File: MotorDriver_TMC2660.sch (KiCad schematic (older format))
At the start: 17 parts, among them U4 TMC2660

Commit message: Routing is complete.
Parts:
- C7: footprint Capacitor_SMD:C_0603_1608Metric -> Capacitor_SMD:C_0402_1005Metric
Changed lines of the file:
@@
 AR Path="/5AC337B6/5ACE1C6D/5ACC0B66/5AC338BF" Ref="U7"  Part="1"
 AR Path="/5AC337B6/5AD9F95A/5AD4B0F5/5AC338BF" Ref="U8"  Part="1"
-F 0 "U4" H 4875 2520 60  0000 C CNN
+F 0 "U8" H 4875 2520 60  0000 C CNN
 F 1 "TMC2660" H 4875 2414 60  0000 C CNN
 F 2 "PrntrBoardV1:TMC2660" H 4900 3600 60  0001 C CNN
@@
 AR Path="/5AC337B6/5ACE1C6D/5ACC0B66/5AC33A94" Ref="C50"  Part="1"
 AR Path="/5AC337B6/5AD9F95A/5AD4B0F5/5AC33A94" Ref="C64"  Part="1"
-F 0 "C7" H 4650 1800 50  0000 L CNN
+F 0 "C64" H 4650 1800 50  0000 L CNN
 F 1 "0.1uF 50V" H 4350 1550 50  0000 L CNN
-F 2 "Capacitor_SMD:C_0603_1608Metric" H 4638 1550 50  0001 C CNN
+F 2 "Capacitor_SMD:C_0402_1005Metric" H 4638 1550 50  0001 C CNN
 F 3 "~" H 4600 1700 50  0001 C CNN
 	1    4600 1700
@@
 AR Path="/5AC337B6/5ACE1C6D/5ACC0B66/5AC33B3C" Ref="C48"  Part="1"
 AR Path="/5AC337B6/5AD9F95A/5AD4B0F5/5AC33B3C" Ref="C62"  Part="1"
-F 0 "C5" H 3050 1750 50  0000 L CNN
+F 0 "C62" H 3050 1750 50  0000 L CNN
 F 1 "10uF 50V" H 2850 1650 50  0000 L CNN
 F 2 "Capacitor_SMD:C_1206_3216Metric" H 3338 1550 50  0001 C CNN
@@
 AR Path="/5AC337B6/5ACE1C6D/5ACC0B66/5AC33B85" Ref="C51"  Part="1"
 AR Path="/5AC337B6/5AD9F95A/5AD4B0F5/5AC33B85" Ref="C65"  Part="1"
-F 0 "C8" V 5098 2100 50  0000 C CNN
+F 0 "C65" V 5098 2100 50  0000 C CNN
 F 1 "0.47uF" V 5189 2100 50  0000 C CNN
 F 2 "Capacitor_SMD:C_0603_1608Metric" H 5388 1950 50  0001 C CNN
@@
 AR Path="/5AC337B6/5ACE1C6D/5ACC0B66/5AC33C56" Ref="C52"  Part="1"
 AR Path="/5AC337B6/5AD9F95A/5AD4B0F5/5AC33C56" Ref="C66"  Part="1"
-F 0 "C9" H 5765 1896 50  0000 L CNN
+F 0 "C66" H 5765 1896 50  0000 L CNN
 F 1 "0.1uF" H 5765 1805 50  0000 L CNN
 F 2 "Capacitor_SMD:C_0603_1608Metric" H 5688 1700 50  0001 C CNN
@@
 AR Path="/5AC337B6/5ACE1C6D/5ACC0B66/5AC33CA1" Ref="C54"  Part="1"
 AR Path="/5AC337B6/5AD9F95A/5AD4B0F5/5AC33CA1" Ref="C73"  Part="1"
-F 0 "C11" V 6300 2600 50  0000 C CNN
+F 0 "C73" V 6300 2600 50  0000 C CNN
 F 1 "1000pF >50V" V 6400 2700 50  0000 C CNN
 F 2 "Capacitor_SMD:C_0603_1608Metric" H 6238 2600 50  0001 C CNN
@@
 AR Path="/5AC337B6/5ACE1C6D/5ACC0B66/5AC33D6E" Ref="C57"  Part="1"
 AR Path="/5AC337B6/5AD9F95A/5AD4B0F5/5AC33D6E" Ref="C74"  Part="1"
-F 0 "C12" V 6300 3000 50  0000 C CNN
+F 0 "C74" V 6300 3000 50  0000 C CNN
 F 1 "1000pF >50V" V 6400 3100 50  0000 C CNN
 F 2 "Capacitor_SMD:C_0603_1608Metric" H 6238 3000 50  0001 C CNN
@@
 AR Path="/5AC337B6/5ACE1C6D/5ACC0B66/5AC33DC1" Ref="C58"  Part="1"
 AR Path="/5AC337B6/5AD9F95A/5AD4B0F5/5AC33DC1" Ref="C75"  Part="1"
-F 0 "C13" V 6300 3700 50  0000 C CNN
+F 0 "C75" V 6300 3700 50  0000 C CNN
 F 1 "1000pF >50V" V 6400 3850 50  0000 C CNN
 F 2 "Capacitor_SMD:C_0603_1608Metric" H 6238 3700 50  0001 C CNN
@@
 AR Path="/5AC337B6/5ACE1C6D/5ACC0B66/5AC33E6E" Ref="C59"  Part="1"
 AR Path="/5AC337B6/5AD9F95A/5AD4B0F5/5AC33E6E" Ref="C76"  Part="1"
-F 0 "C14" V 6300 4150 50  0000 C CNN
+F 0 "C76" V 6300 4150 50  0000 C CNN
 F 1 "1000pF >50V" V 6400 4250 50  0000 C CNN
 F 2 "Capacitor_SMD:C_0603_1608Metric" H 6238 4100 50  0001 C CNN
@@
 AR Path="/5AC337B6/5ACE1C6D/5ACC0B66/5AC33EDF" Ref="C60"  Part="1"
 AR Path="/5AC337B6/5AD9F95A/5AD4B0F5/5AC33EDF" Ref="C77"  Part="1"
-F 0 "C18" H 7300 4550 50  0000 L CNN
+F 0 "C77" H 7300 4550 50  0000 L CNN
 F 1 "0.01uF X7R 10% 50V" H 7550 4550 50  0000 L CNN
 F 2 "Capacitor_SMD:C_0603_1608Metric" H 7238 4400 50  0001 C CNN
@@
 AR Path="/5AC337B6/5ACE1C6D/5ACC0B66/5AC33F7D" Ref="C53"  Part="1"
 AR Path="/5AC337B6/5AD9F95A/5AD4B0F5/5AC33F7D" Ref="C67"  Part="1"
-F 0 "C10" H 5650 5100 50  0000 L CNN
+F 0 "C67" H 5650 5100 50  0000 L CNN
 F 1 "0.01uF X7R 10% 50V" H 4950 5000 50  0000 L CNN
 F 2 "Capacitor_SMD:C_0603_1608Metric" H 5938 4900 50  0001 C CNN
@@
 AR Path="/5AC337B6/5ACE1C6D/5ACC0B66/5AC34593" Ref="#PWR049"  Part="1"
 AR Path="/5AC337B6/5AD9F95A/5AD4B0F5/5AC34593" Ref="#PWR059"  Part="1"
-F 0 "#PWR014" H 5650 1950 50  0001 C CNN
+F 0 "#PWR059" H 5650 1950 50  0001 C CNN
 F 1 "GND" H 5655 2027 50  0000 C CNN
 F 2 "" H 5650 2200 50  0001 C CNN
@@
 AR Path="/5AC337B6/5ACE1C6D/5ACC0B66/5AC345D6" Ref="#PWR048"  Part="1"
 AR Path="/5AC337B6/5AD9F95A/5AD4B0F5/5AC345D6" Ref="#PWR058"  Part="1"
-F 0 "#PWR013" H 3300 1800 50  0001 C CNN
+F 0 "#PWR058" H 3300 1800 50  0001 C CNN
 F 1 "GND" H 3305 1877 50  0000 C CNN
 F 2 "" H 3300 2050 50  0001 C CNN
@@
 AR Path="/5AC337B6/5ACE1C6D/5ACC0B66/5AC34619" Ref="#PWR050"  Part="1"
 AR Path="/5AC337B6/5AD9F95A/5AD4B0F5/5AC34619" Ref="#PWR060"  Part="1"
-F 0 "#PWR015" H 6450 2500 50  0001 C CNN
+F 0 "#PWR060" H 6450 2500 50  0001 C CNN
 F 1 "GND" H 6550 2750 50  0000 C CNN
 F 2 "" H 6450 2750 50  0001 C CNN
@@
 AR Path="/5AC337B6/5ACE1C6D/5ACC0B66/5AC3465C" Ref="#PWR051"  Part="1"
 AR Path="/5AC337B6/5AD9F95A/5AD4B0F5/5AC3465C" Ref="#PWR061"  Part="1"
-F 0 "#PWR016" H 6450 2900 50  0001 C CNN
+F 0 "#PWR061" H 6450 2900 50  0001 C CNN
 F 1 "GND" H 6550 3050 50  0000 C CNN
 F 2 "" H 6450 3150 50  0001 C CNN
@@
 AR Path="/5AC337B6/5ACE1C6D/5ACC0B66/5AC3469F" Ref="#PWR052"  Part="1"
 AR Path="/5AC337B6/5AD9F95A/5AD4B0F5/5AC3469F" Ref="#PWR062"  Part="1"
-F 0 "#PWR017" H 6450 3600 50  0001 C CNN
+F 0 "#PWR062" H 6450 3600 50  0001 C CNN
 F 1 "GND" H 6550 3850 50  0000 C CNN
 F 2 "" H 6450 3850 50  0001 C CNN
@@
 AR Path="/5AC337B6/5ACE1C6D/5ACC0B66/5AC346E2" Ref="#PWR053"  Part="1"
 AR Path="/5AC337B6/5AD9F95A/5AD4B0F5/5AC346E2" Ref="#PWR063"  Part="1"
-F 0 "#PWR018" H 6450 4000 50  0001 C CNN
+F 0 "#PWR063" H 6450 4000 50  0001 C CNN
 F 1 "GND" H 6550 4250 50  0000 C CNN
 F 2 "" H 6450 4250 50  0001 C CNN
@@
 AR Path="/5AC337B6/5ACE1C6D/5ACC0B66/5AC34725" Ref="#PWR047"  Part="1"
 AR Path="/5AC337B6/5AD9F95A/5AD4B0F5/5AC34725" Ref="#PWR057"  Part="1"
-F 0 "#PWR012" H 2950 6050 50  0001 C CNN
+F 0 "#PWR057" H 2950 6050 50  0001 C CNN
 F 1 "GND" H 2955 6127 50  0000 C CNN
 F 2 "" H 2950 6300 50  0001 C CNN
@@
 AR Path="/5AC337B6/5ACE1C6D/5ACC0B66/5AC3912E" Ref="R58"  Part="1"
 AR Path="/5AC337B6/5AD9F95A/5AD4B0F5/5AC3912E" Ref="R62"  Part="1"
-F 0 "R2" H 6050 4950 50  0000 L CNN
+F 0 "R62" H 6050 4950 50  0000 L CNN
 F 1 "22R" H 6050 4850 50  0000 L CNN
 F 2 "Resistor_SMD:R_0603_1608Metric" V 6180 4900 50  0001 C CNN
@@
 AR Path="/5AC337B6/5ACE1C6D/5ACC0B66/5AC391BE" Ref="R59"  Part="1"
 AR Path="/5AC337B6/5AD9F95A/5AD4B0F5/5AC391BE" Ref="R63"  Part="1"
-F 0 "R3" H 6320 5396 50  0000 L CNN
+F 0 "R63" H 6320 5396 50  0000 L CNN
 F 1 "0R051" H 6320 5305 50  0000 L CNN
 F 2 "Resistor_SMD:R_1206_3216Metric" V 6180 5350 50  0001 C CNN
@@
 AR Path="/5AC337B6/5ACE1C6D/5ACC0B66/5AC3921D" Ref="R60"  Part="1"
 AR Path="/5AC337B6/5AD9F95A/5AD4B0F5/5AC3921D" Ref="R64"  Part="1"
-F 0 "R4" H 7300 3900 50  0000 L CNN
+F 0 "R64" H 7300 3900 50  0000 L CNN
 F 1 "22R" H 7300 3800 50  0000 L CNN
 F 2 "Resistor_SMD:R_0603_1608Metric" V 7430 3850 50  0001 C CNN
@@
 AR Path="/5AC337B6/5ACE1C6D/5ACC0B66/5AC392A1" Ref="R61"  Part="1"
 AR Path="/5AC337B6/5AD9F95A/5AD4B0F5/5AC392A1" Ref="R65"  Part="1"
-F 0 "R5" H 7570 5196 50  0000 L CNN
+F 0 "R65" H 7570 5196 50  0000 L CNN
 F 1 "0R051" H 7570 5105 50  0000 L CNN
 F 2 "Resistor_SMD:R_1206_3216Metric" V 7430 5150 50  0001 C CNN
@@
 AR Path="/5AC337B6/5ACE1C6D/5ACC0B66/5AC55FA7" Ref="C49"  Part="1"
 AR Path="/5AC337B6/5AD9F95A/5AD4B0F5/5AC55FA7" Ref="C63"  Part="1"
-F 0 "C6" H 3700 1900 50  0000 L CNN
+F 0 "C63" H 3700 1900 50  0000 L CNN
 F 1 "100uF 35V" H 3700 1800 50  0000 L CNN
 F 2 "Capacitor_SMD:CP_Elec_6.3x7.7" H 3650 1700 50  0001 C CNN
@@
 AR Path="/5AC337B6/5ACE1C6D/5ACC0B66/5ACA36B2" Ref="C47"  Part="1"
 AR Path="/5AC337B6/5AD9F95A/5AD4B0F5/5ACA36B2" Ref="C61"  Part="1"
-F 0 "C4" H 2715 1746 50  0000 L CNN
+F 0 "C61" H 2715 1746 50  0000 L CNN
 F 1 "10uF 50V" H 2650 1550 50  0000 L CNN
 F 2 "Capacitor_SMD:C_1206_3216Metric" H 2638 1550 50  0001 C CNN

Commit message: Add missing files from the TMC2130 branch.
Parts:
- C10, C11, C12, C13, C14, C18, C8, C9: footprint Capacitor_SMD:C_0603_1608Metric -> PrntrBoardV1:C_0603_1608Metric
- C4, C5: footprint Capacitor_SMD:C_1206_3216Metric -> PrntrBoardV1:C_1206_3216Metric
- C7: footprint Capacitor_SMD:C_0402_1005Metric -> PrntrBoardV1:C_0402_1005Metric
- R2, R4: footprint Resistor_SMD:R_0603_1608Metric -> PrntrBoardV1:R_0603_1608Metric
- R3, R5: footprint Resistor_SMD:R_1206_3216Metric -> PrntrBoardV1:R_1206_3216Metric
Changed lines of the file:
@@
 F 0 "C64" H 4650 1800 50  0000 L CNN
 F 1 "0.1uF 50V" H 4350 1550 50  0000 L CNN
-F 2 "Capacitor_SMD:C_0402_1005Metric" H 4638 1550 50  0001 C CNN
+F 2 "PrntrBoardV1:C_0402_1005Metric" H 4638 1550 50  0001 C CNN
 F 3 "~" H 4600 1700 50  0001 C CNN
 	1    4600 1700
@@
 F 0 "C62" H 3050 1750 50  0000 L CNN
 F 1 "10uF 50V" H 2850 1650 50  0000 L CNN
-F 2 "Capacitor_SMD:C_1206_3216Metric" H 3338 1550 50  0001 C CNN
+F 2 "PrntrBoardV1:C_1206_3216Metric" H 3338 1550 50  0001 C CNN
 F 3 "~" H 3300 1700 50  0001 C CNN
 	1    3300 1700
@@
 F 0 "C65" V 5098 2100 50  0000 C CNN
 F 1 "0.47uF" V 5189 2100 50  0000 C CNN
-F 2 "Capacitor_SMD:C_0603_1608Metric" H 5388 1950 50  0001 C CNN
+F 2 "PrntrBoardV1:C_0603_1608Metric" H 5388 1950 50  0001 C CNN
 F 3 "~" H 5350 2100 50  0001 C CNN
 	1    5350 2100
@@
 F 0 "C66" H 5765 1896 50  0000 L CNN
 F 1 "0.1uF" H 5765 1805 50  0000 L CNN
-F 2 "Capacitor_SMD:C_0603_1608Metric" H 5688 1700 50  0001 C CNN
+F 2 "PrntrBoardV1:C_0603_1608Metric" H 5688 1700 50  0001 C CNN
 F 3 "~" H 5650 1850 50  0001 C CNN
 	1    5650 1850
@@
 F 0 "C73" V 6300 2600 50  0000 C CNN
 F 1 "1000pF >50V" V 6400 2700 50  0000 C CNN
-F 2 "Capacitor_SMD:C_0603_1608Metric" H 6238 2600 50  0001 C CNN
+F 2 "PrntrBoardV1:C_0603_1608Metric" H 6238 2600 50  0001 C CNN
 F 3 "~" H 6200 2750 50  0001 C CNN
 	1    6200 2750
@@
 F 0 "C74" V 6300 3000 50  0000 C CNN
 F 1 "1000pF >50V" V 6400 3100 50  0000 C CNN
-F 2 "Capacitor_SMD:C_0603_1608Metric" H 6238 3000 50  0001 C CNN
+F 2 "PrntrBoardV1:C_0603_1608Metric" H 6238 3000 50  0001 C CNN
 F 3 "~" H 6200 3150 50  0001 C CNN
 	1    6200 3150
@@
 F 0 "C75" V 6300 3700 50  0000 C CNN
 F 1 "1000pF >50V" V 6400 3850 50  0000 C CNN
-F 2 "Capacitor_SMD:C_0603_1608Metric" H 6238 3700 50  0001 C CNN
+F 2 "PrntrBoardV1:C_0603_1608Metric" H 6238 3700 50  0001 C CNN
 F 3 "~" H 6200 3850 50  0001 C CNN
 	1    6200 3850
@@
 F 0 "C76" V 6300 4150 50  0000 C CNN
 F 1 "1000pF >50V" V 6400 4250 50  0000 C CNN
-F 2 "Capacitor_SMD:C_0603_1608Metric" H 6238 4100 50  0001 C CNN
+F 2 "PrntrBoardV1:C_0603_1608Metric" H 6238 4100 50  0001 C CNN
 F 3 "~" H 6200 4250 50  0001 C CNN
 	1    6200 4250
@@
 F 0 "C77" H 7300 4550 50  0000 L CNN
 F 1 "0.01uF X7R 10% 50V" H 7550 4550 50  0000 L CNN
-F 2 "Capacitor_SMD:C_0603_1608Metric" H 7238 4400 50  0001 C CNN
+F 2 "PrntrBoardV1:C_0603_1608Metric" H 7238 4400 50  0001 C CNN
 F 3 "~" H 7200 4550 50  0001 C CNN
 	1    7200 4550
@@
 F 0 "C67" H 5650 5100 50  0000 L CNN
 F 1 "0.01uF X7R 10% 50V" H 4950 5000 50  0000 L CNN
-F 2 "Capacitor_SMD:C_0603_1608Metric" H 5938 4900 50  0001 C CNN
+F 2 "PrntrBoardV1:C_0603_1608Metric" H 5938 4900 50  0001 C CNN
 F 3 "~" H 5900 5050 50  0001 C CNN
 	1    5900 5050
@@
 F 0 "R62" H 6050 4950 50  0000 L CNN
 F 1 "22R" H 6050 4850 50  0000 L CNN
-F 2 "Resistor_SMD:R_0603_1608Metric" V 6180 4900 50  0001 C CNN
+F 2 "PrntrBoardV1:R_0603_1608Metric" V 6180 4900 50  0001 C CNN
 F 3 "~" H 6250 4900 50  0001 C CNN
 	1    6250 4900
@@
 F 0 "R63" H 6320 5396 50  0000 L CNN
 F 1 "0R051" H 6320 5305 50  0000 L CNN
-F 2 "Resistor_SMD:R_1206_3216Metric" V 6180 5350 50  0001 C CNN
+F 2 "PrntrBoardV1:R_1206_3216Metric" V 6180 5350 50  0001 C CNN
 F 3 "~" H 6250 5350 50  0001 C CNN
 	1    6250 5350
@@
 F 0 "R64" H 7300 3900 50  0000 L CNN
 F 1 "22R" H 7300 3800 50  0000 L CNN
-F 2 "Resistor_SMD:R_0603_1608Metric" V 7430 3850 50  0001 C CNN
+F 2 "PrntrBoardV1:R_0603_1608Metric" V 7430 3850 50  0001 C CNN
 F 3 "~" H 7500 3850 50  0001 C CNN
 	1    7500 3850
@@
 F 0 "R65" H 7570 5196 50  0000 L CNN
 F 1 "0R051" H 7570 5105 50  0000 L CNN
-F 2 "Resistor_SMD:R_1206_3216Metric" V 7430 5150 50  0001 C CNN
+F 2 "PrntrBoardV1:R_1206_3216Metric" V 7430 5150 50  0001 C CNN
 F 3 "~" H 7500 5150 50  0001 C CNN
 	1    7500 5150
@@
 F 0 "C61" H 2715 1746 50  0000 L CNN
 F 1 "10uF 50V" H 2650 1550 50  0000 L CNN
-F 2 "Capacitor_SMD:C_1206_3216Metric" H 2638 1550 50  0001 C CNN
+F 2 "PrntrBoardV1:C_1206_3216Metric" H 2638 1550 50  0001 C CNN
 F 3 "~" H 2600 1700 50  0001 C CNN
 	1    2600 1700

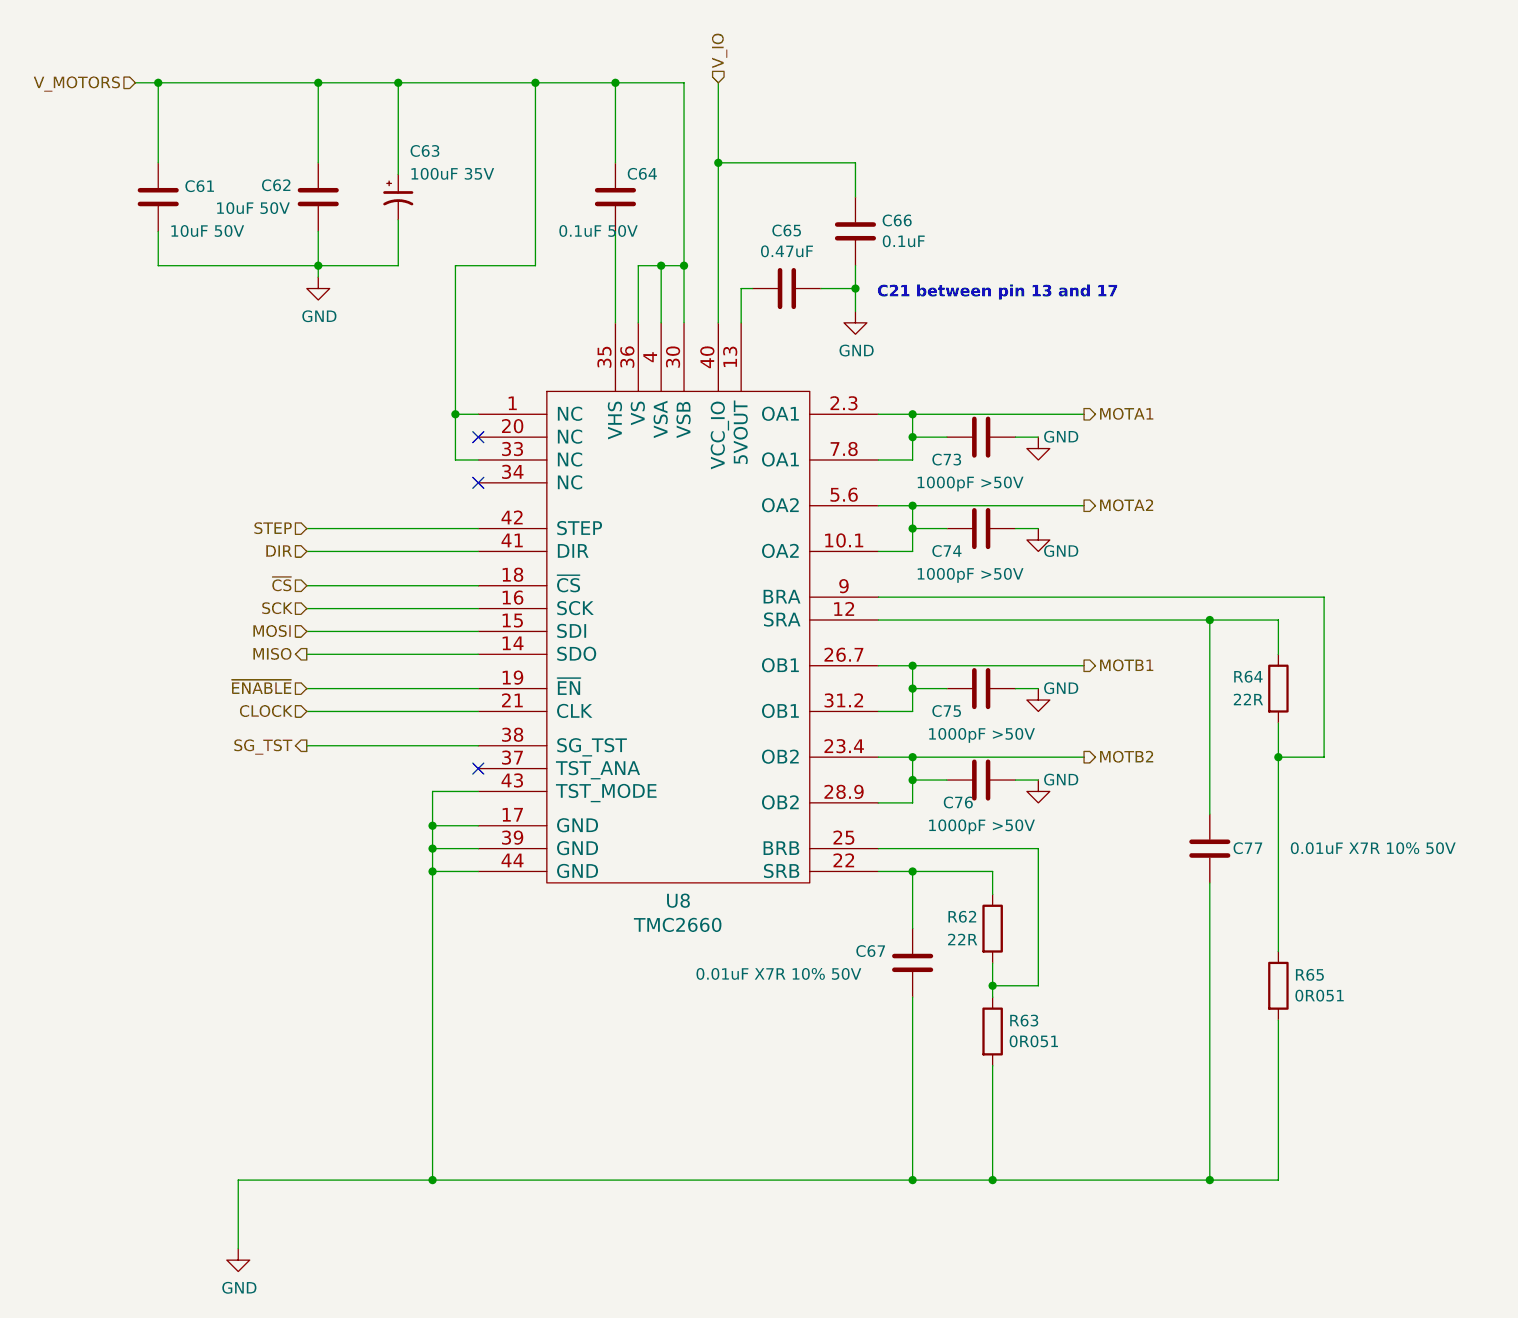
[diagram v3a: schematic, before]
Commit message: Update schematics to match rev3 of tmc2130 branch.
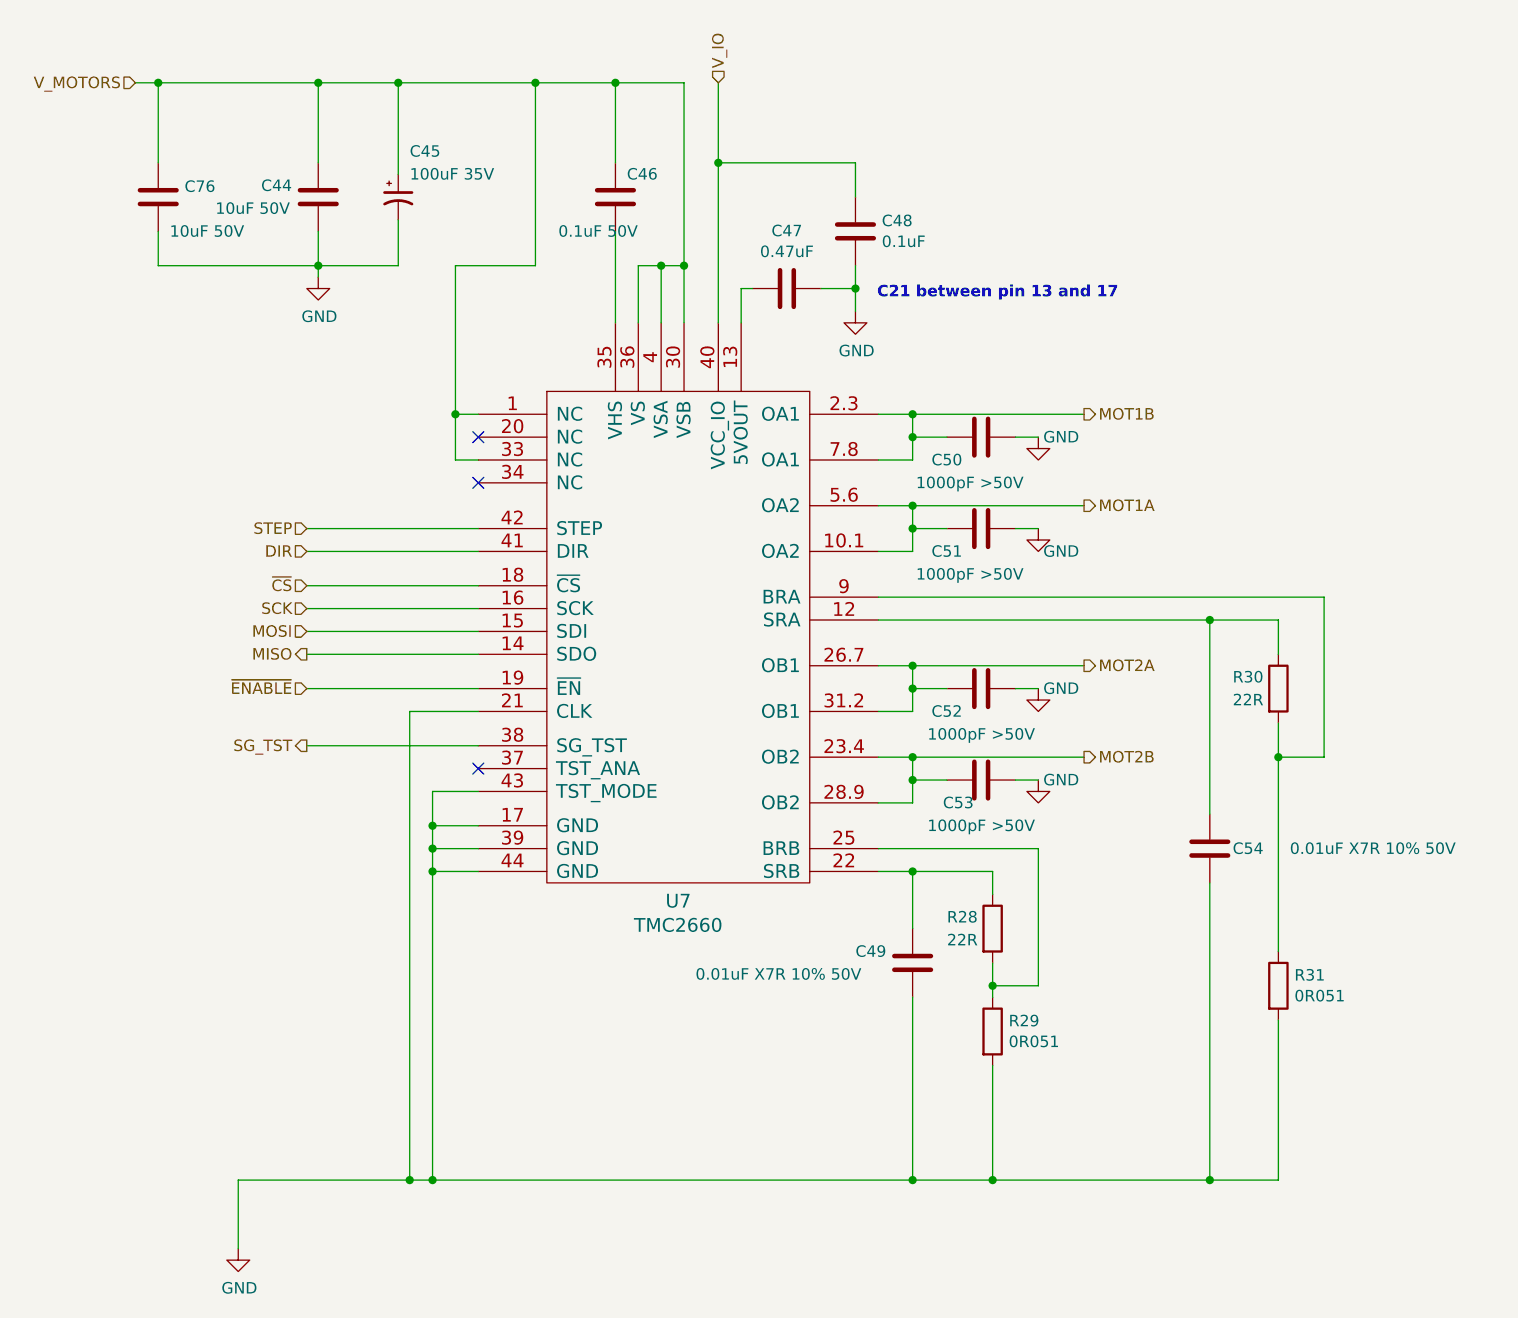
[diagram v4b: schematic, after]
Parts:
- C6: renamed from C7; footprint PrntrBoardV1:C_0402_1005Metric -> PrntrBoardV1:C_0603_1608Metric
- renumbered C11 to C10, C12 to C11, C13 to C12, C14 to C13, C18 to C14, C5 to C4, C6 to C5, C8 to C7, C4 to C74, C9 to C8, C10 to C9
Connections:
- net CLOCK is gone; now on net GND: U4.21 (CLK)
- net MOTA1 renamed MOT1B
- net MOTA2 renamed MOT1A
- net MOTB1 renamed MOT2A
- net MOTB2 renamed MOT2B
